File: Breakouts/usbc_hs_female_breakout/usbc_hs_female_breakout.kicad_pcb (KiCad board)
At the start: 2 copper layers, 15 x 14 mm, 2 parts, among them J1 USB_C_Receptacle, J2 Conn_02x10_Odd_Even

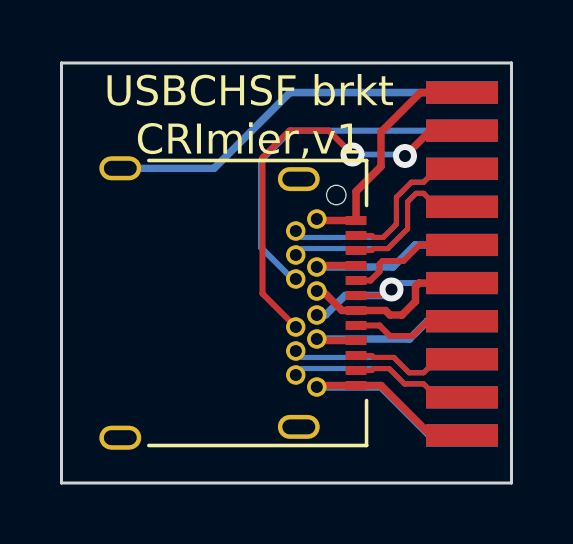
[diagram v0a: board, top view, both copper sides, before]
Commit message: usbc_hs_female_breakout: WIP v2, ever so slightly better routing (iirc?), increased socket compat
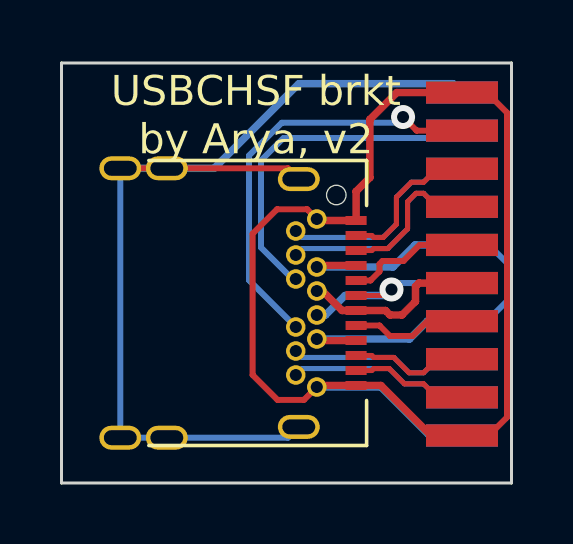
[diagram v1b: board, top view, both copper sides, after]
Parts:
- J1: footprint Connector_USB:USB_C_Receptacle_Amphenol_12401548E4-2A -> usbc_hs_female_breakout:USB_C_Receptacle_Amphenol_12401548E4-2A
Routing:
- net GND: track 18.9 -> 43.1 mm
- net SHD: track 12.4 -> 33.9 mm
- net VBUS: track 12.9 -> 17.7 mm
- net CC2: track 13.8 -> 14.2 mm, vias 2 -> 1
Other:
- board text added: "USBCHSF brkt by Arya, v2"
- board text removed: "USBCHSF brkt CRImier,v1"
- board text removed: "USBCHSF brkt by CRImier, v1"
